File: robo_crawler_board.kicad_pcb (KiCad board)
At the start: 2 copper layers, 13 parts, among them J1 Screw_Terminal_01x02, J2 Screw_Terminal_01x02, J3 Screw_Terminal_01x02, U4 DRV8871DDA, U5 DRV8871DDA

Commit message: rev3 pcb done except ground planes
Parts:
- added ?: , , F.Cu at (193.7, 115.7)
- added ?: , , F.Cu at (196.2, 114.4)
- added ?: , , F.Cu at (195.0, 117.0)
- added ?: , , F.Cu at (198.7, 115.7)
- added ?: , , F.Cu at (163.2, 114.2)
- added ?: , , F.Cu at (156.9, 116.8)
- added ?: , , F.Cu at (197.5, 117.0)
- added ?: , , F.Cu at (158.2, 115.5)
- added ?: , , F.Cu at (195.0, 114.4)
- added ?: , , F.Cu at (196.2, 115.7)
- added ?: , , F.Cu at (200.0, 115.7)
- added ?: , , F.Cu at (159.4, 116.8)
- added ?: , , F.Cu at (193.7, 114.4)
- added ?: , , F.Cu at (197.5, 114.4)
- added ?: , , F.Cu at (159.4, 114.2)
- added ?: , , F.Cu at (160.8, 114.2)
- added ?: , , F.Cu at (198.7, 117.0)
- added ?: , , F.Cu at (156.9, 114.2)
- added ?: , , F.Cu at (161.9, 116.8)
- added ?: , , F.Cu at (161.9, 115.5)
- added ?: , , F.Cu at (200.0, 117.0)
- added ?: , , F.Cu at (158.2, 116.8)
- added ?: , , F.Cu at (160.8, 115.5)
- added ?: , , F.Cu at (156.9, 115.5)
- added ?: , , F.Cu at (163.2, 116.8)
- added ?: , , F.Cu at (163.2, 115.5)
- added ?: , , F.Cu at (196.2, 117.0)
- added ?: , , F.Cu at (197.5, 115.7)
- added ?: , , F.Cu at (198.7, 114.4)
- added ?: , , F.Cu at (158.2, 114.2)
- added ?: , , F.Cu at (195.0, 115.7)
- added ?: , , F.Cu at (200.0, 114.4)
- added ?: , , F.Cu at (160.8, 116.8)
- added ?: , , F.Cu at (159.4, 115.5)
- added ?: , , F.Cu at (193.7, 117.0)
- added ?: , , F.Cu at (161.9, 114.2)
- added C1: 100nF, Capacitor_SMD:C_0805_2012Metric, F.Cu at (148.3, 100.5)
- added C10: 100nF, Capacitor_SMD:C_0805_2012Metric, F.Cu at (147.6, 65.5)
- added C11: 10µF, Capacitor_SMD:C_0805_2012Metric, F.Cu at (142.5, 65.5)
- added C12: 10µF, Capacitor_SMD:C_0805_2012Metric, F.Cu at (141.4, 83.2)
- added C13: 100nF, Capacitor_SMD:C_0805_2012Metric, F.Cu at (146.3, 83.2)
- added C14: 1000µF, Capacitor_THT:CP_Radial_D10.0mm_P5.00mm, F.Cu at (222.0, 108.1)
- added C15: 100nF, Capacitor_SMD:C_0805_2012Metric, F.Cu at (215.5, 110.8)
- added C16: 100nF, Capacitor_SMD:C_0805_2012Metric, F.Cu at (141.3, 110.3)
- added C2: 220nF, Capacitor_SMD:C_0805_2012Metric, F.Cu at (168.9, 118.4)
- added C3: 220nF, Capacitor_SMD:C_0805_2012Metric, F.Cu at (168.9, 112.8)
- added C4: 1nF, Capacitor_SMD:C_0805_2012Metric, F.Cu at (141.8, 100.5)
- added C5: 100nF, Capacitor_SMD:C_0805_2012Metric, F.Cu at (214.2, 102.2)
- added C6: 1nF, Capacitor_SMD:C_0805_2012Metric, F.Cu at (207.0, 102.2)
- added C7: 220nF, Capacitor_SMD:C_0805_2012Metric, F.Cu at (189.2, 112.8)
- added C8: 220nF, Capacitor_SMD:C_0805_2012Metric, F.Cu at (189.2, 118.5)
- added C9: 1000µF, Capacitor_THT:CP_Radial_D10.0mm_P5.00mm, F.Cu at (134.6, 113.0)
- added J4: Screw_Terminal_01x02, TerminalBlock:TerminalBlock_bornier-2_P5.08mm, F.Cu at (181.6, 119.4)
- added R10: 1k, Resistor_SMD:R_0805_2012Metric, F.Cu at (209.8, 102.2)
- added R11: 10k, Resistor_SMD:R_0805_2012Metric, F.Cu at (167.4, 71.0)
- added R3: 10k, Resistor_SMD:R_0805_2012Metric, F.Cu at (167.3, 62.2)
- added R5: 512, Resistor_SMD:R_0805_2012Metric, F.Cu at (145.8, 100.4)
- added R6: 1k, Resistor_SMD:R_0805_2012Metric, F.Cu at (139.2, 100.5)
- added R7: 10k, Resistor_SMD:R_0805_2012Metric, F.Cu at (167.5, 79.5)
- added R9: 512, Resistor_SMD:R_0805_2012Metric, F.Cu at (216.8, 102.2)
- added U2: IFX007T, ifx007t half-bridge:TO127P1500X440-8N, F.Cu at (200.7, 115.6)
- added U6: IFX007T, ifx007t half-bridge:TO127P1500X440-8N, F.Cu at (156.2, 115.6)
- moved R2 104.3 mm to (154.2, 68.2), turned to 90 degrees
- moved U5 86.3 mm to (147.9, 71.2), turned to 180 degrees
- moved U4 76.9 mm to (146.7, 88.9), turned to 180 degrees
- moved U1 72.0 mm to (196.8, 69.8), turned to 180 degrees
- moved J2 71.6 mm to (133.5, 84.4), turned to -90 degrees
- moved J3 69.8 mm to (133.3, 66.0), turned to -90 degrees
- moved H1 66.7 mm to (132.0, 58.2)
- moved H4 60.1 mm to (132.0, 121.0)
- moved U3 58.1 mm to (180.3, 96.5)
- moved J1 57.6 mm to (219.7, 92.7), turned to 90 degrees
- moved H2 23.0 mm to (224.8, 58.2)
- moved R1 21.4 mm to (152.5, 85.8), turned to 90 degrees
- moved H3 20.4 mm to (224.8, 121.0)
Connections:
- J1 pad 2: +18V -> +12V
- U1 pad 30: DRIVE_CH1 -> Net-(U1-IO18)
- U1 pad 31: DRIVE_CH2 -> Net-(U1-IO19)
- U1 pad 36: MOTOR1_CH1 -> unconnected-(U1-IO22-Pad36)
- U1 pad 37: MOTOR1_CH2 -> Net-(U1-IO23)
- U1 pad 8: unconnected-(U1-IO32-Pad8) -> MOTOR1_CH1
- U1 pad 9: unconnected-(U1-IO33-Pad9) -> MOTOR1_CH2
- U3 pad 2: +18V -> +12V
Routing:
- net +12V: track 0.00 -> 273.4 mm
- net DRIVE_EN: track 0.00 -> 147.4 mm, vias 0 -> 4
- net GND: track 0.00 -> 88.8 mm
- net DRIVE_CH2: track 0.00 -> 82.0 mm, vias 0 -> 2
- net +5V: track 0.00 -> 69.1 mm
- net DRIVE_CH1: track 0.00 -> 67.8 mm, vias 0 -> 2
- net MOTOR2_CH2: track 0.00 -> 53.1 mm, vias 0 -> 2
- net MOTOR2_CH1: track 0.00 -> 52.7 mm, vias 0 -> 2
- net MOTOR1_CH2: track 0.00 -> 46.7 mm, vias 0 -> 1
- net MOTOR1_CH1: track 0.00 -> 43.4 mm, vias 0 -> 1
- net Net-(U1-IO19): track 0.00 -> 40.9 mm
- net Net-(U1-IO18): track 0.00 -> 28.4 mm, vias 0 -> 1
- net Net-(U6-IS): track 0.00 -> 26.3 mm, vias 0 -> 2
- net Net-(J4-Pin_2): track 0.00 -> 21.8 mm
- net Net-(U6-SR): track 0.00 -> 21.5 mm, vias 0 -> 2
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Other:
- board text added: "+V"
- board text added: "-V"
- board text added: "OpenWCB"

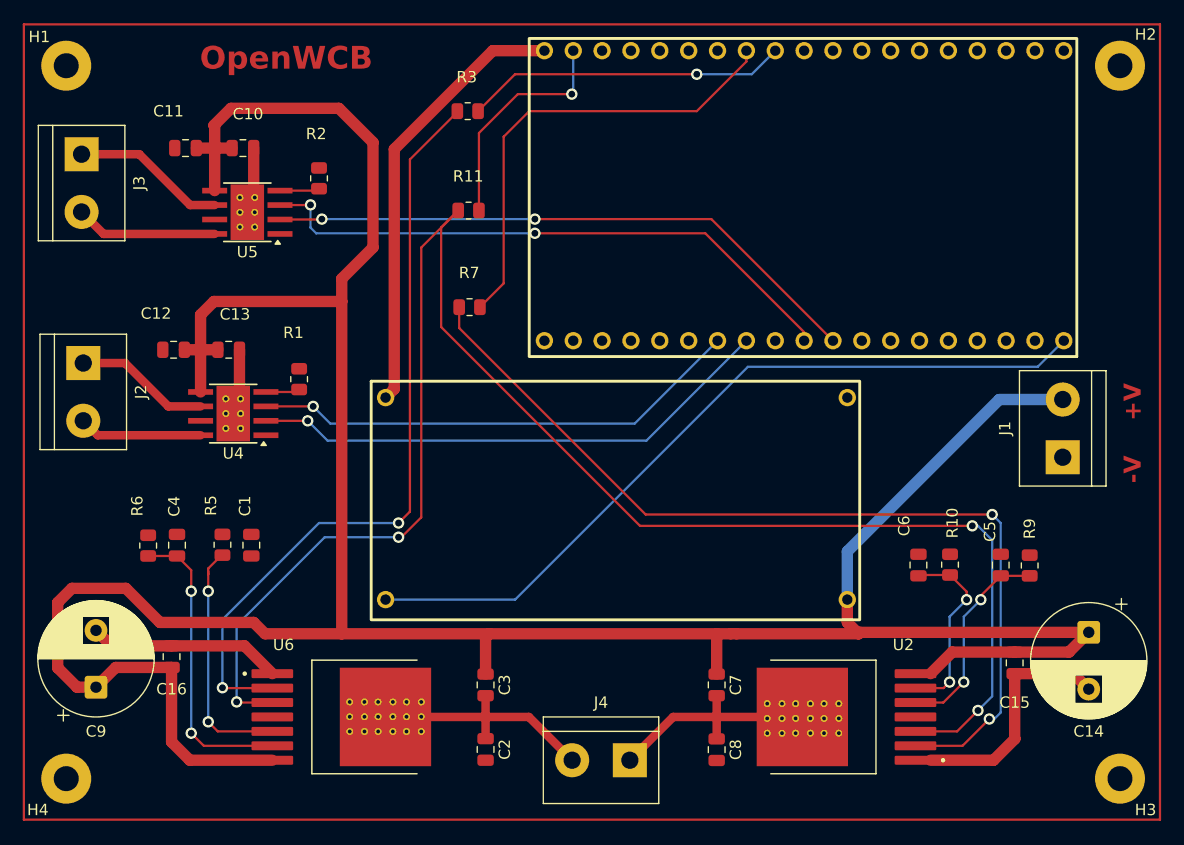
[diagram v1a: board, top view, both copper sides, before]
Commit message: added ground planes, drc errors need to be fixed
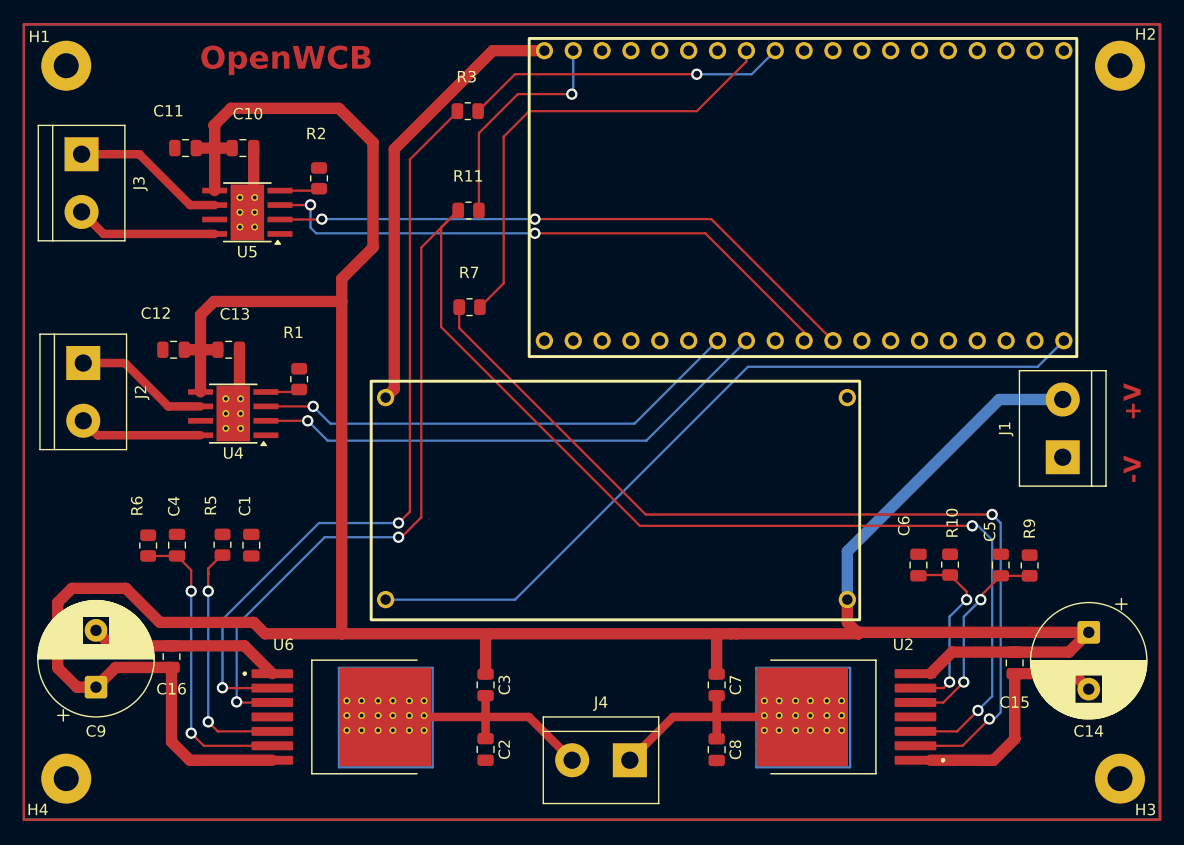
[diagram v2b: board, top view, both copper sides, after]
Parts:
- removed the ? at (193.7, 115.7)
- removed the ? at (196.2, 114.4)
- removed the ? at (195.0, 117.0)
- removed the ? at (198.7, 115.7)
- removed the ? at (163.2, 114.2)
- removed the ? at (156.9, 116.8)
- removed the ? at (197.5, 117.0)
- removed the ? at (158.2, 115.5)
- removed the ? at (195.0, 114.4)
- removed the ? at (196.2, 115.7)
- removed the ? at (200.0, 115.7)
- removed the ? at (159.4, 116.8)
- removed the ? at (193.7, 114.4)
- removed the ? at (197.5, 114.4)
- removed the ? at (159.4, 114.2)
- removed the ? at (160.8, 114.2)
- removed the ? at (198.7, 117.0)
- removed the ? at (156.9, 114.2)
- removed the ? at (161.9, 116.8)
- removed the ? at (161.9, 115.5)
- removed the ? at (200.0, 117.0)
- removed the ? at (158.2, 116.8)
- removed the ? at (160.8, 115.5)
- removed the ? at (156.9, 115.5)
- removed the ? at (163.2, 116.8)
- removed the ? at (163.2, 115.5)
- removed the ? at (196.2, 117.0)
- removed the ? at (197.5, 115.7)
- removed the ? at (198.7, 114.4)
- removed the ? at (158.2, 114.2)
- removed the ? at (195.0, 115.7)
- removed the ? at (200.0, 114.4)
- removed the ? at (160.8, 116.8)
- removed the ? at (159.4, 115.5)
- removed the ? at (193.7, 117.0)
- removed the ? at (161.9, 114.2)
- added ?: , , F.Cu at (163.5, 116.8)
- added ?: , , F.Cu at (158.0, 115.5)
- added ?: , , F.Cu at (194.8, 115.5)
- added ?: , , F.Cu at (197.5, 116.8)
- added ?: , , F.Cu at (162.2, 115.5)
- added ?: , , F.Cu at (193.4, 114.2)
- added ?: , , F.Cu at (197.5, 115.5)
- added ?: , , F.Cu at (163.5, 115.5)
- added ?: , , F.Cu at (198.9, 114.2)
- added ?: , , F.Cu at (194.8, 116.8)
- added ?: , , F.Cu at (158.0, 116.8)
- added ?: , , F.Cu at (200.2, 116.8)
- added ?: , , F.Cu at (158.0, 114.2)
- added ?: , , F.Cu at (198.9, 116.8)
- added ?: , , F.Cu at (193.4, 115.5)
- added ?: , , F.Cu at (196.2, 116.8)
- added ?: , , F.Cu at (160.8, 116.8)
- added ?: , , F.Cu at (160.8, 114.2)
- added ?: , , F.Cu at (156.7, 114.2)
- added ?: , , F.Cu at (156.7, 116.8)
- added ?: , , F.Cu at (196.2, 115.5)
- added ?: , , F.Cu at (162.2, 116.8)
- added ?: , , F.Cu at (200.2, 114.2)
- added ?: , , F.Cu at (163.5, 114.2)
- added ?: , , F.Cu at (159.4, 115.5)
- added ?: , , F.Cu at (159.4, 114.2)
- added ?: , , F.Cu at (194.8, 114.2)
- added ?: , , F.Cu at (196.2, 114.2)
- added ?: , , F.Cu at (200.2, 115.5)
- added ?: , , F.Cu at (193.4, 116.8)
- added ?: , , F.Cu at (198.9, 115.5)
- added ?: , , F.Cu at (197.5, 114.2)
- added ?: , , F.Cu at (160.8, 115.5)
- added ?: , , F.Cu at (156.7, 115.5)
- added ?: , , F.Cu at (159.4, 116.8)
- added ?: , , F.Cu at (162.2, 114.2)
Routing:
- added copper zone on B.Cu, net GND
- added copper zone on F.Cu, net GND
- added copper zone on B.Cu, net Net-(J4-Pin_1)
- added copper zone on B.Cu, net Net-(J4-Pin_2)

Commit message: resolved drc errors
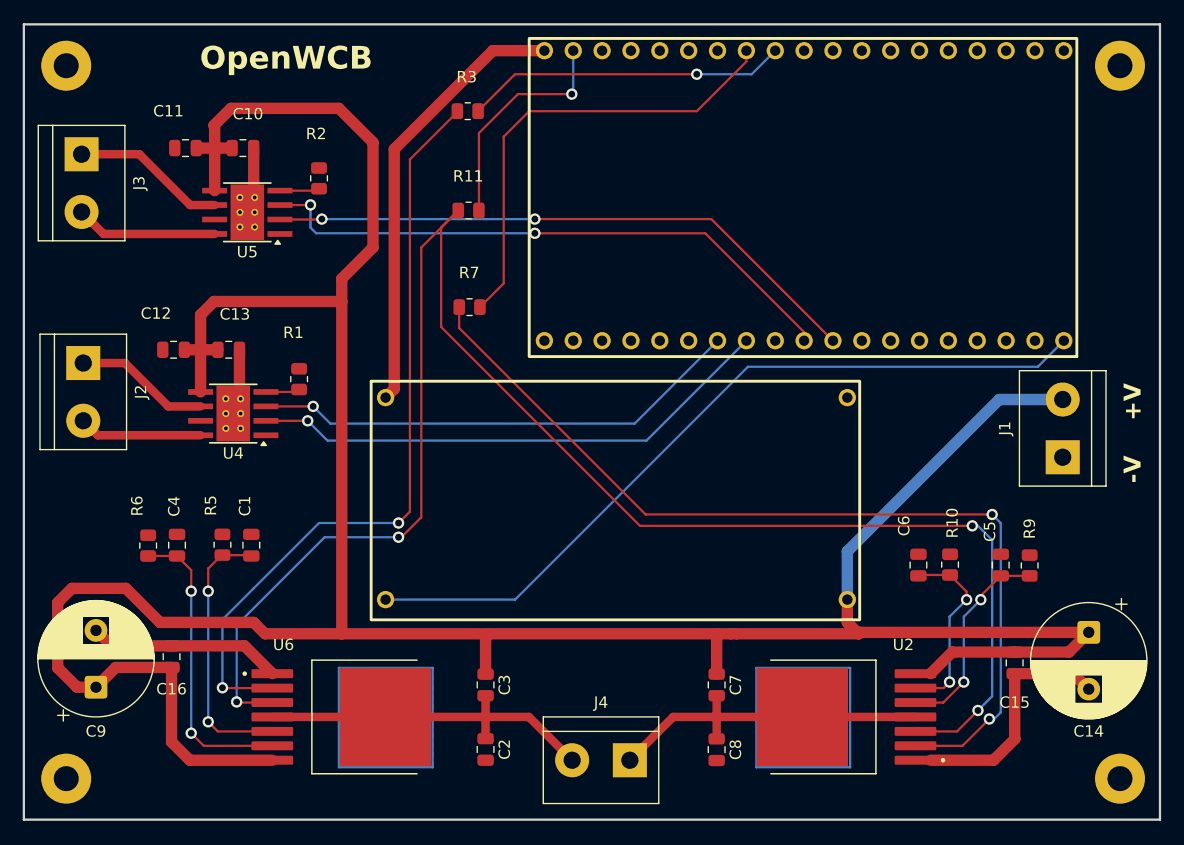
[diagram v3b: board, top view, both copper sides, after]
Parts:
- removed ? (x36): , 
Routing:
- net Net-(J4-Pin_2): track 21.8 -> 31.7 mm
- net Net-(J4-Pin_1): track 20.6 -> 30.6 mm
- net Net-(U6-SR): track 21.5 -> 23.8 mm
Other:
- board outline added: 100 x 70 mm

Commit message: production rev3
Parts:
- R5, R9: value 512 -> 510
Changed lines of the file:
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@@
 			)
 		)
-		(property "LCSC Part Number" ""
+		(property "LCSC Part Number" "C83170"
 			(at 0 0 180)
 			(unlocked yes)
@@
 		(sheetname "/")
 		(sheetfile "robo_crawler_board.kicad_sch")
-		(attr through_hole)
+		(attr through_hole exclude_from_bom dnp)
 		(fp_line
 			(start 7.62 3.81)
@@
 			)
 		)
-		(property "LCSC Part Number" ""
+		(property "LCSC Part Number" "C513710"
 			(at 0 0 270)
 			(unlocked yes)
@@
 		(sheetname "/")
 		(sheetfile "robo_crawler_board.kicad_sch")
-		(attr through_hole)
+		(attr through_hole exclude_from_bom dnp)
 		(fp_line
 			(start 7.62 -3.81)
@@
 			)
 		)
-		(property "Description" "Unpolarized capacitor"
+		(property "Description" "polarized capacitor"
 			(at 0 0 90)
 			(layer "F.Fab")
@@
 			)
 		)
-		(property "LCSC Part Number" ""
+		(property "LCSC Part Number" "C49678"
 			(at 0 0 0)
 			(unlocked yes)
@@
 			)
 		)
-		(property "Value" "512"
+		(property "Value" "510"
 			(at -3.9125 -0.25 270)
 			(layer "F.Fab")
@@
 			)
 		)
-		(property "LCSC Part Number" "C2076395"
+		(property "LCSC Part Number" "C2907333"
 			(at 0 0 270)
 			(unlocked yes)
@@
 			)
 		)
-		(property "LCSC Part Number" ""
+		(property "LCSC Part Number" "C513710"
 			(at 0 0 270)
 			(unlocked yes)
@@
 		(sheetname "/")
 		(sheetfile "robo_crawler_board.kicad_sch")
-		(attr through_hole)
+		(attr through_hole exclude_from_bom dnp)
 		(fp_line
 			(start -2.54 3.81)
@@
 			)
 		)
-		(property "LCSC Part Number" ""
+		(property "LCSC Part Number" "C49678"
 			(at 0 0 0)
 			(unlocked yes)
@@
 			)
 		)
-		(property "Description" "Unpolarized capacitor"
+		(property "Description" "polarized capacitor"
 			(at 0 0 90)
 			(layer "F.Fab")
@@
 		(sheetname "/")
 		(sheetfile "robo_crawler_board.kicad_sch")
-		(attr through_hole)
+		(attr through_hole exclude_from_bom dnp)
 		(fp_line
 			(start -2.54 3.81)
@@
 			)
 		)
-		(property "LCSC Part Number" ""
+		(property "LCSC Part Number" "C51210"
 			(at 0 0 90)
 			(unlocked yes)
@@
 			)
 		)
-		(property "LCSC Part Number" ""
+		(property "LCSC Part Number" "C51210"
 			(at 0 0 90)
 			(unlocked yes)
@@
 		(sheetname "/")
 		(sheetfile "robo_crawler_board.kicad_sch")
+		(attr exclude_from_bom dnp)
 		(fp_rect
 			(start -24.1 -14)
@@
 			)
 		)
-		(property "LCSC Part Number" ""
+		(property "LCSC Part Number" "C49678"
 			(at 0 0 90)
 			(unlocked yes)
@@
 			)
 		)
-		(property "LCSC Part Number" ""
+		(property "LCSC Part Number" "C49678"
 			(at 0 0 90)
 			(unlocked yes)
@@
 			)
 		)
-		(property "LCSC Part Number" ""
+		(property "LCSC Part Number" "C513710"
 			(at 0 0 270)
 			(unlocked yes)
@@
 			)
 		)
-		(property "LCSC Part Number" ""
+		(property "LCSC Part Number" "C513710"
 			(at 0 0 270)
 			(unlocked yes)
@@
 			)
 		)
-		(property "Value" "512"
+		(property "Value" "510"
 			(at -3.7975 -1.27 90)
 			(layer "F.Fab")
@@
 			)
 		)
-		(property "LCSC Part Number" "C2076395"
+		(property "LCSC Part Number" "C2907333"
 			(at 0 0 270)
 			(unlocked yes)
@@
 			)
 		)
-		(property "LCSC Part Number" ""
+		(property "LCSC Part Number" "C83170"
 			(at 0 0 180)
 			(unlocked yes)
@@
 			)
 		)
-		(property "LCSC Part Number" ""
+		(property "LCSC Part Number" "C49678"
 			(at 0 0 90)
 			(unlocked yes)
@@
 		(sheetname "/")
 		(sheetfile "robo_crawler_board.kicad_sch")
+		(attr exclude_from_bom dnp)
 		(fp_rect
 			(start -21.5 -10.5)
@@
 			)
 		)
-		(property "LCSC Part Number" ""
+		(property "LCSC Part Number" "C49678"
 			(at 0 0 270)
 			(unlocked yes)
